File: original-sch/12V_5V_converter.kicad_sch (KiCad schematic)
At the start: 1 part

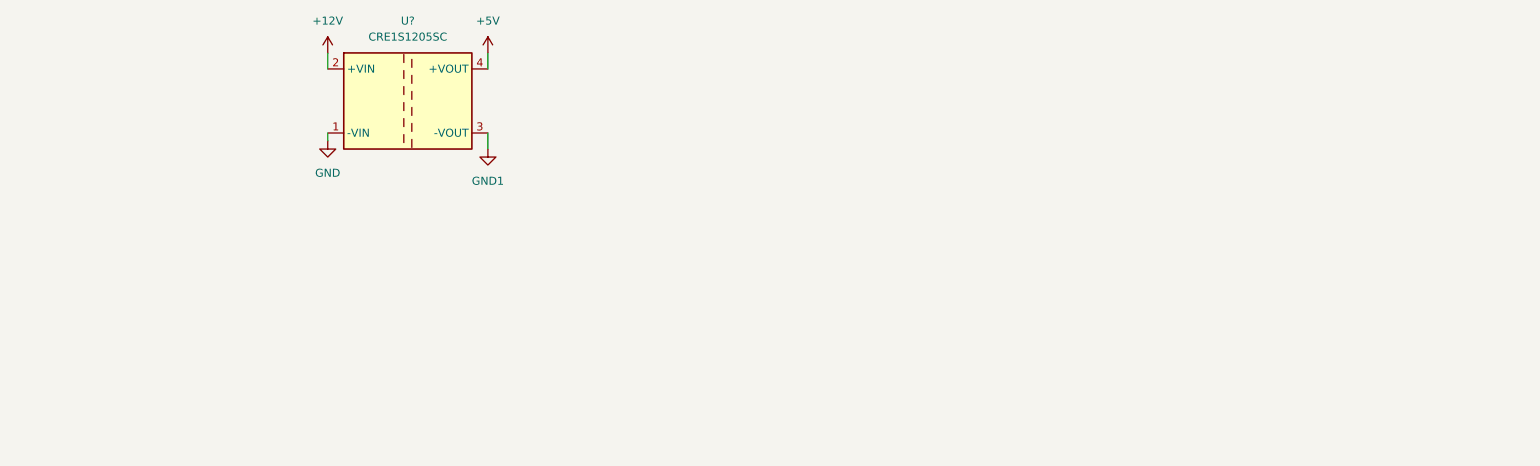
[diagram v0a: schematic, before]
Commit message: Add in thermistor and ADC
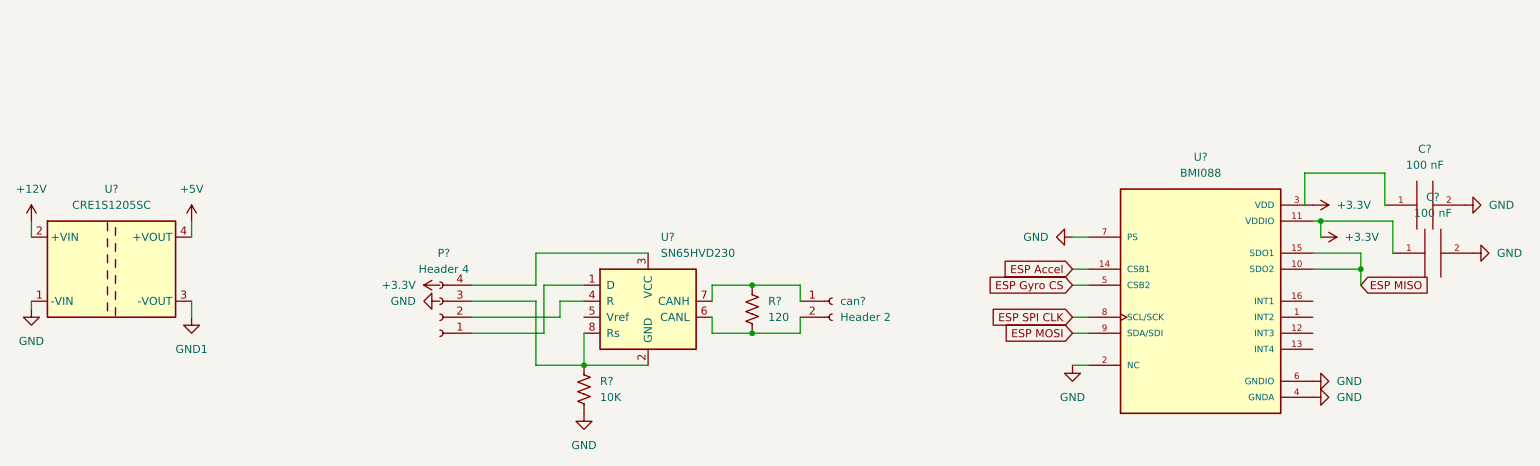
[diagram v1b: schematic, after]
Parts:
- added C? (x2): 100 nF, symbol pspice:CAP
- added P?: Header 4, symbol Connector:Conn_01x04_Female
- added R?: 120, symbol Device:R_US
- added R?: 10K, symbol Device:R_US
- added U?: SN65HVD230, Package_SO:SOIC-8_3.9x4.9mm_P1.27mm, symbol Interface_CAN_LIN:SN65HVD230
- added U?: BMI088, PQFN50P450X300X100-16N, symbol BMI088:BMI088
- added can?: Header 2, symbol Connector:Conn_01x02_Female
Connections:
- net GND: now also C?.2, C?.2, R?.2, U?.2 (NC), U?.4 (GNDA), U?.6 (GNDIO), U?.7 (PS)
- new net: P?.1 (Pin_1), U?.1 (D)
- new net: P?.2 (Pin_2), U?.4 (R)
- new net: P?.3 (Pin_3), R?.1, U?.2 (GND), U?.8 (Rs)
- new net: P?.4 (Pin_4), U?.3 (VCC)
- new net: R?.1, U?.7 (CANH), can?.1 (Pin_1)
- new net: R?.2, U?.6 (CANL), can?.2 (Pin_2)
- new net +3.3V: C?.1, U?.11 (VDDIO), U?.3 (VDD)
- new net ESP Accel : U?.14 (CSB1)
- new net ESP Gyro CS: U?.5 (CSB2)
- new net ESP MISO: U?.10 (SDO2), U?.15 (SDO1)
- new net ESP MOSI: U?.9 (SDA/SDI)
- new net ESP SPI CLK: U?.8 (SCL/SCK)
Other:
- moved on the sheet: U?
